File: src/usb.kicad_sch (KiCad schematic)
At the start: 16 parts, among them J3 USB_C_Receptacle_USB2.0_14P, J4 USB_C_Receptacle_USB2.0_14P, J5 USB_C_Receptacle_USB2.0_14P, U1 ECP5U_12_CABGA256, U5 TPD2EUSB30, U6 TPD2EUSB30, U7 FT231XQ, U8 TPD2EUSB30

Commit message: Rev 2
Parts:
- added D2: GREEN, LED_SMD:LED_0603_1608Metric, symbol Device:LED_ALT
- added D3: YELLOW, LED_SMD:LED_0603_1608Metric, symbol Device:LED_ALT
- added JP1: Jumper_3_Bridged12, Jumper:SolderJumper-3_P1.3mm_Bridged2Bar12_RoundedPad1.0x1.5mm, symbol Jumper:Jumper_3_Bridged12
- added R25, R26: 549, Resistor_SMD:R_0603_1608Metric, symbol Device:R
- D1: LCSC Part (none) -> C2286
- R1, R2, R3, R4, R6, R7: LCSC Part (none) -> C23186
- R5: LCSC Part (none) -> C23204
- U5, U6, U8: LCSC Part (none) -> C2844720
- U7: LCSC Part (none) -> C132159
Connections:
- net FT2V5: now also JP1.1 (A); no longer U7.11 (~{RESET})
- net GND: now also JP1.3 (B), R25.1, R26.1
- net LED2: now reaches U1.D14 (PR2D/-/RDQ8)
- net LED2: now also D3.2 (A)
- new net: D3.1 (K), R26.2
- new net: JP1.2 (C), U7.11 (~{RESET})
- new net: D2.1 (K), R25.2
- new net LED1: D2.2 (A)
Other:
- moved on the sheet: U8

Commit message: Tidy project
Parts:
- D1: JLCPCB Part # (none) -> C2286; LCSC Part C2286 -> (none)
- D2: JLCPCB Part # (none) -> C2994781; LCSC Part C2994781 -> (none)
- D3: JLCPCB Part # (none) -> C72038; LCSC Part C72038 -> (none)
- J3, J4, J5: JLCPCB Part # (none) -> C2765186; LCSC Part C2765186 -> (none)
- R1, R2, R3, R4, R6, R7: JLCPCB Part # (none) -> C23186; LCSC Part C23186 -> (none)
- R25, R26, R5: JLCPCB Part # (none) -> C23204; LCSC Part C23204 -> (none)
- U1: JLCPCB Part # (none) -> C1521614; LCSC Part C1521614 -> (none)
- U5, U6, U8: JLCPCB Part # (none) -> C2844720; LCSC Part C2844720 -> (none)
- U7: JLCPCB Part # (none) -> C132159; LCSC Part C132159 -> (none)
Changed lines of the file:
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@@
 			)
 		)
-		(property "LCSC Part" "C2286"
+		(property "JLCPCB Part #" "C2286"
 			(at 142.24 104.14 0)
 			(effects
@@
 					(size 1.27 1.27)
 				)
-				(hide yes)
 			)
 		)
@@
 			)
 		)
-		(property "LCSC Part" "C23204"
+		(property "JLCPCB Part #" "C23204"
 			(at 166.37 104.14 0)
 			(effects
@@
 			)
 		)
-		(property "LCSC Part" "C23186"
+		(property "JLCPCB Part #" "C23186"
 			(at 59.69 96.52 0)
 			(effects
@@
 			)
 		)
-		(property "LCSC Part" "C23204"
+		(property "JLCPCB Part #" "C23204"
 			(at 166.37 129.54 0)
 			(effects
@@
 			)
 		)
-		(property "LCSC Part" " C1521614"
+		(property "JLCPCB Part #" " C1521614"
 			(at 142.24 167.64 0)
 			(effects
@@
 					(size 1.27 1.27)
 				)
-				(hide yes)
 			)
 		)
@@
 			)
 		)
-		(property "LCSC Part" "C132159"
+		(property "JLCPCB Part #" "C132159"
 			(at 111.76 48.26 0)
 			(effects
@@
 			)
 		)
-		(property "LCSC Part" "C23204"
+		(property "JLCPCB Part #" "C23204"
 			(at 166.37 121.92 0)
 			(effects
@@
 			)
 		)
-		(property "LCSC Part" "C23186"
+		(property "JLCPCB Part #" "C23186"
 			(at 59.69 33.02 0)
 			(effects
@@
 			)
 		)
-		(property "LCSC Part" "C23186"
+		(property "JLCPCB Part #" "C23186"
 			(at 59.69 93.98 0)
 			(effects
@@
 			)
 		)
-		(property "LCSC Part" "C23186"
+		(property "JLCPCB Part #" "C23186"
 			(at 59.69 30.48 0)
 			(effects
@@
 			)
 		)
-		(property "LCSC Part" "C72038"
+		(property "JLCPCB Part #" "C72038"
 			(at 142.24 129.54 0)
 			(effects
@@
 					(size 1.27 1.27)
 				)
-				(hide yes)
 			)
 		)
@@
 			)
 		)
-		(property "LCSC Part" "C2844720"
+		(property "JLCPCB Part #" "C2844720"
 			(at 91.44 105.41 0)
 			(effects
@@
 			)
 		)
-		(property "LCSC Part" "C23186"
+		(property "JLCPCB Part #" "C23186"
 			(at 59.69 157.48 0)
 			(effects
@@
 			)
 		)
-		(property "LCSC Part" " C2765186"
+		(property "JLCPCB Part #" " C2765186"
 			(at 40.64 40.64 0)
 			(effects
@@
 					(size 1.27 1.27)
 				)
-				(hide yes)
 			)
 		)
@@
 			)
 		)
-		(property "LCSC Part" ""
-			(at 87.63 55.88 0)
-			(effects
-				(font
-					(size 1.27 1.27)
-				)
-				(hide yes)
-			)
-		)
 		(pin "3"
 		)
@@
 			)
 		)
-		(property "LCSC Part" "C23186"
+		(property "JLCPCB Part #" "C23186"
 			(at 59.69 154.94 0)
 			(effects
@@
 			)
 		)
-		(property "LCSC Part" " C2765186"
+		(property "JLCPCB Part #" " C2765186"
 			(at 40.64 165.1 0)
 			(effects
@@
 					(size 1.27 1.27)
 				)
-				(hide yes)
 			)
 		)
@@
 			)
 		)
-		(property "LCSC Part" "C2844720"
+		(property "JLCPCB Part #" "C2844720"
 			(at 64.77 66.04 0)
 			(effects
@@
 			)
 		)
-		(property "LCSC Part" "C2994781"
+		(property "JLCPCB Part #" "C2994781"
 			(at 142.24 121.92 0)
 			(effects
@@
 					(size 1.27 1.27)
 				)
-				(hide yes)
 			)
 		)
@@
 			)
 		)
-		(property "LCSC Part" " C1521614"
+		(property "JLCPCB Part #" " C1521614"
 			(at 234.95 78.74 0)
 			(effects
@@
 					(size 1.27 1.27)
 				)
-				(hide yes)
 			)
 		)
@@
 			)
 		)
-		(property "LCSC Part" "C2844720"
+		(property "JLCPCB Part #" "C2844720"
 			(at 92.71 166.37 0)
 			(effects
@@
 			)
 		)
-		(property "LCSC Part" " C2765186"
+		(property "JLCPCB Part #" " C2765186"
 			(at 40.64 104.14 0)
 			(effects
@@
 					(size 1.27 1.27)
 				)
-				(hide yes)
 			)
 		)

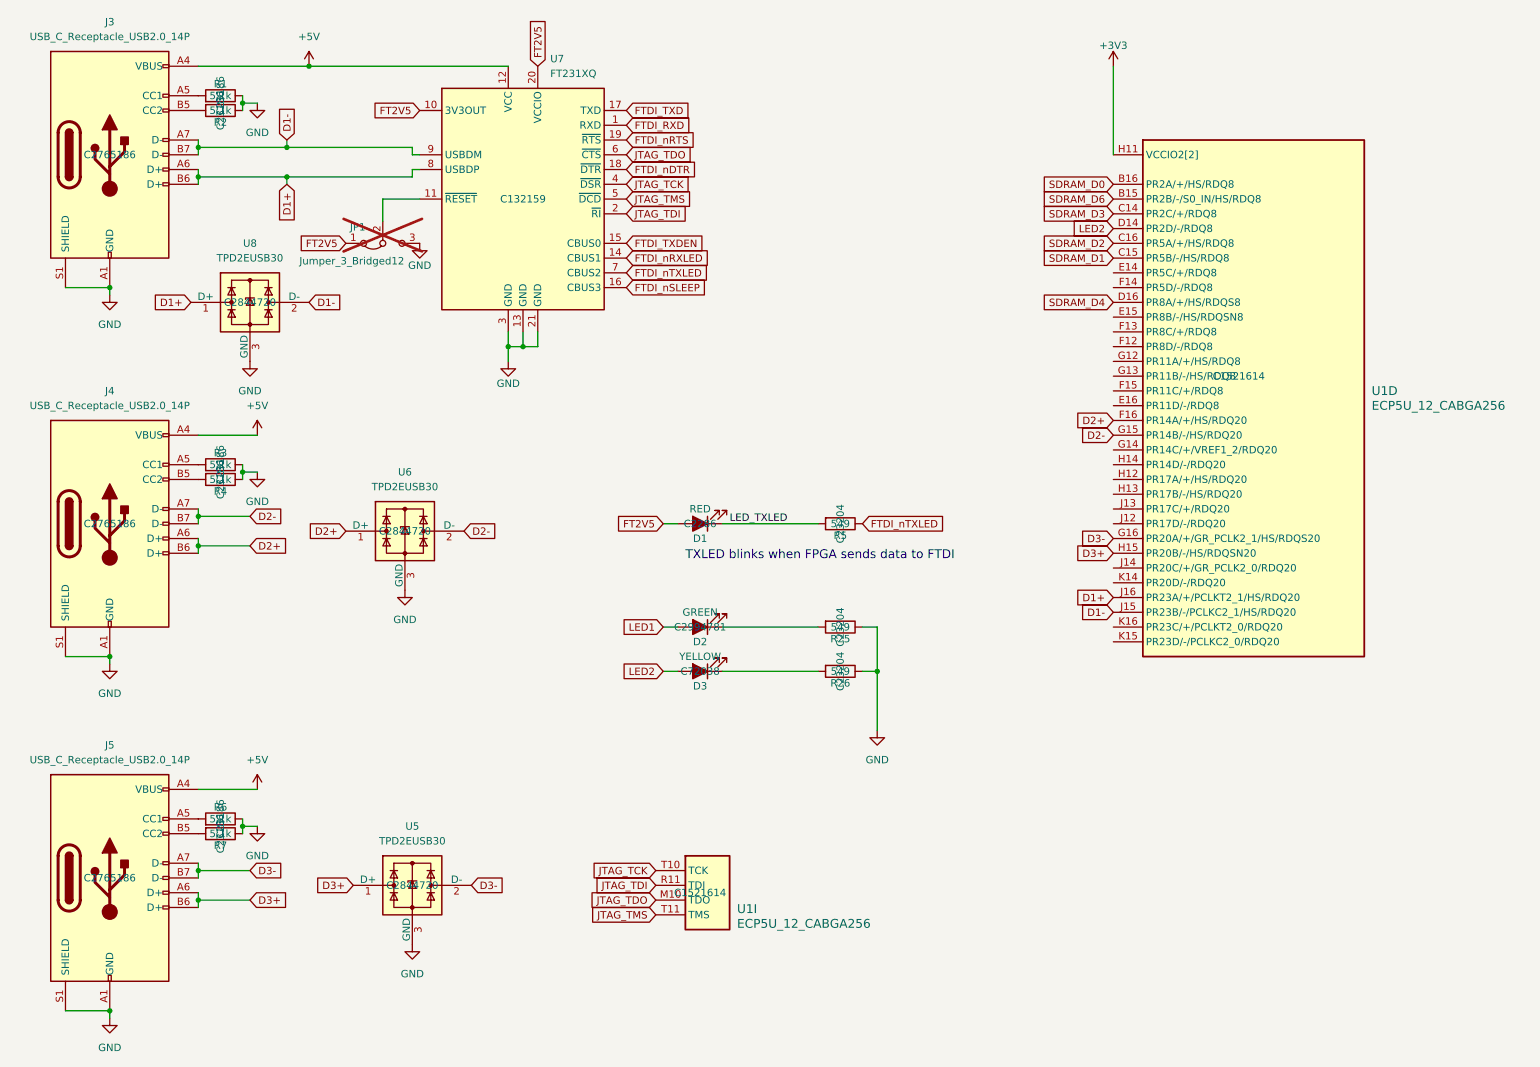
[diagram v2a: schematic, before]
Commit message: Add test points
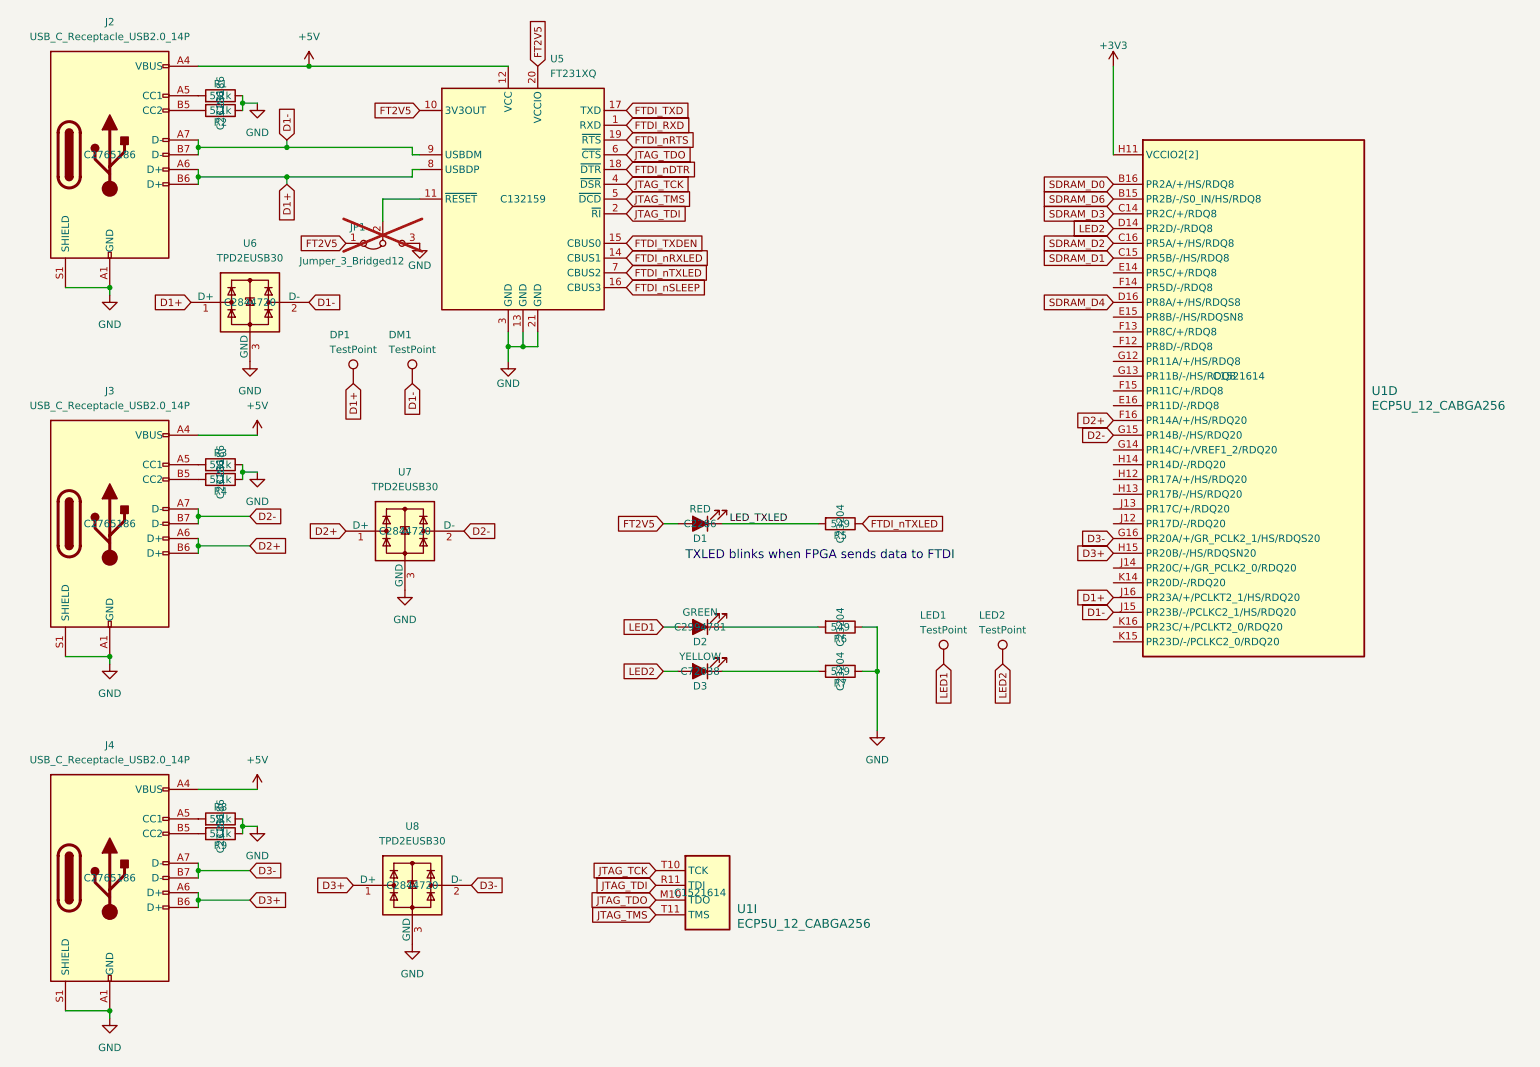
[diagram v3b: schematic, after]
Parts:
- added DM1, DP1, LED1, LED2: TestPoint, TestPoint:TestPoint_Pad_D1.5mm, symbol Connector:TestPoint
- renumbered J3 to J2, J4 to J3, J5 to J4, R25 to R6, R26 to R7, R6 to R8, R7 to R9, U7 to U5, U8 to U6, U6 to U7, U5 to U8
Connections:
- net D1+: now also DP1.1
- net D1-: now also DM1.1
- net LED1: now also LED1.1
- net LED2: now also LED2.1
